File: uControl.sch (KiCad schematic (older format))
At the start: 3 parts, among them U501 MCP4802-E/SN

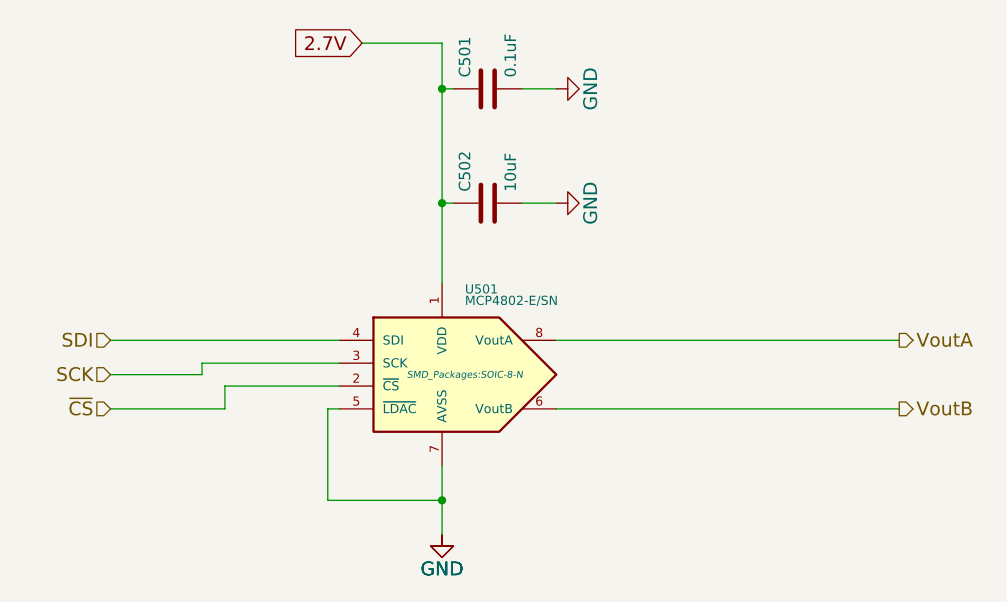
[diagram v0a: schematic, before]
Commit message: updated schematic with part numbers to ICs
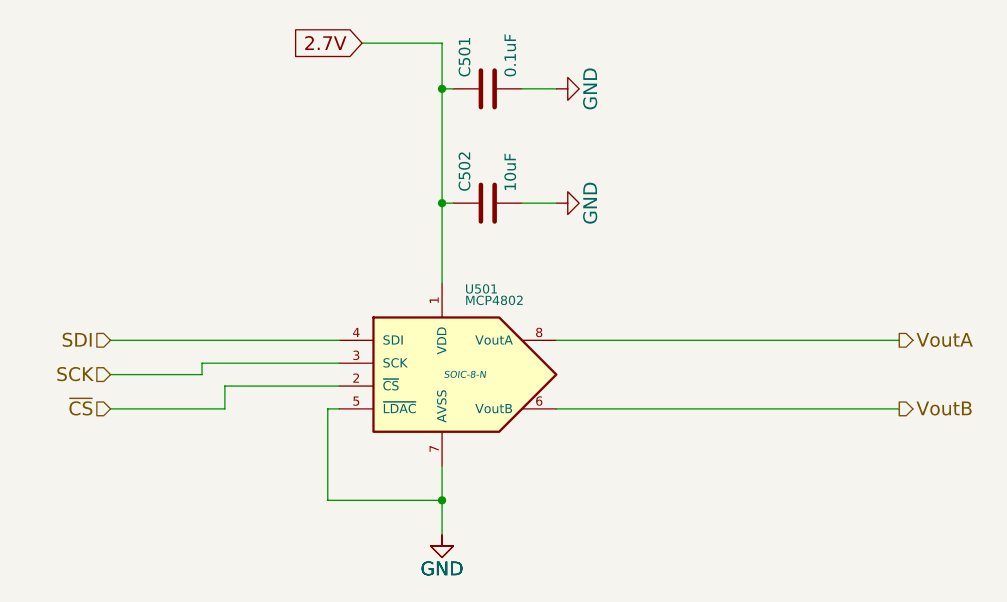
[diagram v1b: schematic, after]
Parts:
- U501: value MCP4802-E/SN -> MCP4802; footprint SMD_Packages:SOIC-8-N -> SOIC-8-N; MPN (none) -> MCP4802-E/SN
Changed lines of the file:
@@
 P 5650 4350
 F 0 "U501" H 5650 4700 40  0000 L BNN
-F 1 "MCP4802-E/SN" H 5650 4650 40  0000 L BNN
-F 2 "SMD_Packages:SOIC-8-N" H 5650 4350 30  0000 C CIN
-F 3 "" H 5650 4350 60  0000 C CNN
+F 1 "MCP4802" H 5650 4650 40  0000 L BNN
+F 2 "SOIC-8-N" H 5650 4350 30  0000 C CIN
+F 3 "http://ww1.microchip.com/downloads/en/DeviceDoc/22249A.pdf" H 5650 4350 60  0001 C CNN
+F 4 "MCP4802-E/SN" H 5650 4350 60  0001 C CNN "MPN"
 	1    5650 4350
 	1    0    0    -1
